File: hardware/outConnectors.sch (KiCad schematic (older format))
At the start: 4 parts, among them P4 CONN_01X04, P5 CONN_01X04

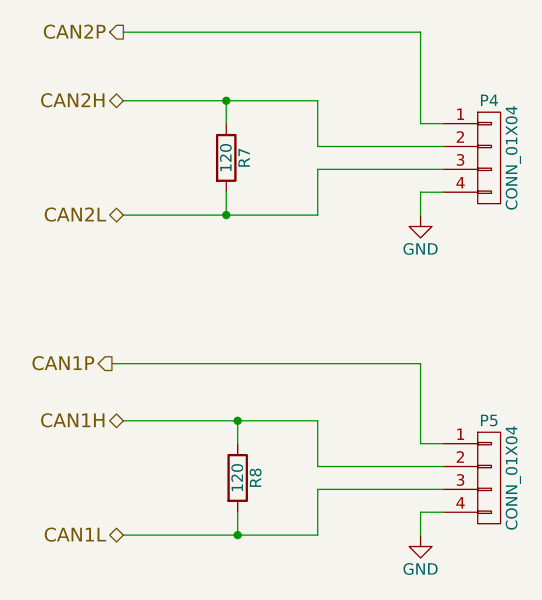
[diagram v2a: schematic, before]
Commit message: Fixed some warnings (like unconnected pins)
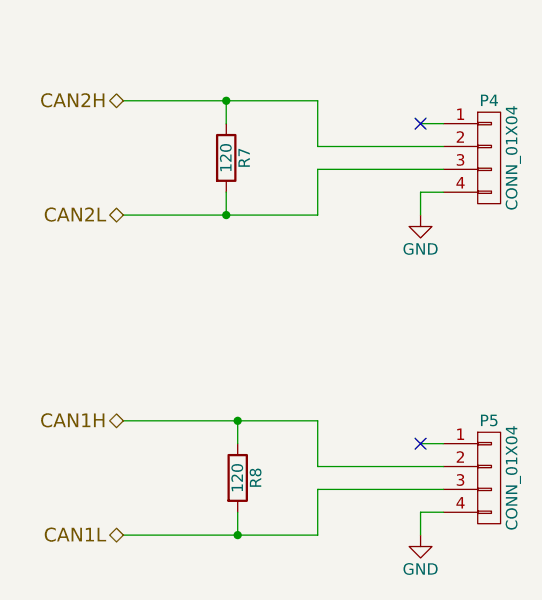
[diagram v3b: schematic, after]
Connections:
- net CAN1P: no longer names the net of P5.1 (P1)
- net CAN2P: no longer names the net of P4.1 (P1)
- no-connect marks 0 -> 2
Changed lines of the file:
@@
 	4300 3900 4300 4100
 $Comp
-L GND #PWR031
+L GND #PWR032
 U 1 1 5619AC3E
 P 4750 4100
-F 0 "#PWR031" H 4750 3850 50  0001 C CNN
+F 0 "#PWR032" H 4750 3850 50  0001 C CNN
 F 1 "GND" H 4750 3950 50  0000 C CNN
 F 2 "" H 4750 4100 60  0000 C CNN
@@
 	4750 4000 4850 4000
 $Comp
-L GND #PWR032
+L GND #PWR033
 U 1 1 5619AC9B
 P 4750 2700
-F 0 "#PWR032" H 4750 2450 50  0001 C CNN
+F 0 "#PWR033" H 4750 2450 50  0001 C CNN
 F 1 "GND" H 4750 2550 50  0000 C CNN
 F 2 "" H 4750 2700 60  0000 C CNN
@@
 	4750 2600 4850 2600
 Wire Wire Line
-	4750 1900 4750 2300
-Wire Wire Line
 	4750 2300 4850 2300
-Wire Wire Line
-	4750 3350 4750 3700
 Wire Wire Line
 	4750 3700 4850 3700
 Wire Wire Line
 	3900 2600 3900 2700
-Text HLabel 3450 1900 0    60   Output ~ 0
-CAN2P
-Text HLabel 3400 3350 0    60   Output ~ 0
-CAN1P
-Wire Wire Line
-	3450 1900 4750 1900
-Wire Wire Line
-	4750 3350 3400 3350
+NoConn ~ 4750 2300
+NoConn ~ 4750 3700
 $EndSCHEMATC
